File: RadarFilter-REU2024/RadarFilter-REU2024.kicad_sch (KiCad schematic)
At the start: 33 parts, among them J1 73099-0, J2 73099-0, J2 Conn_01x04_Pin, J3 73099-0, J6 CONSMA002, J7 CONSMA002, J8 CONSMA002, J9 CONSMA002, U2 ADA4807-2ARM

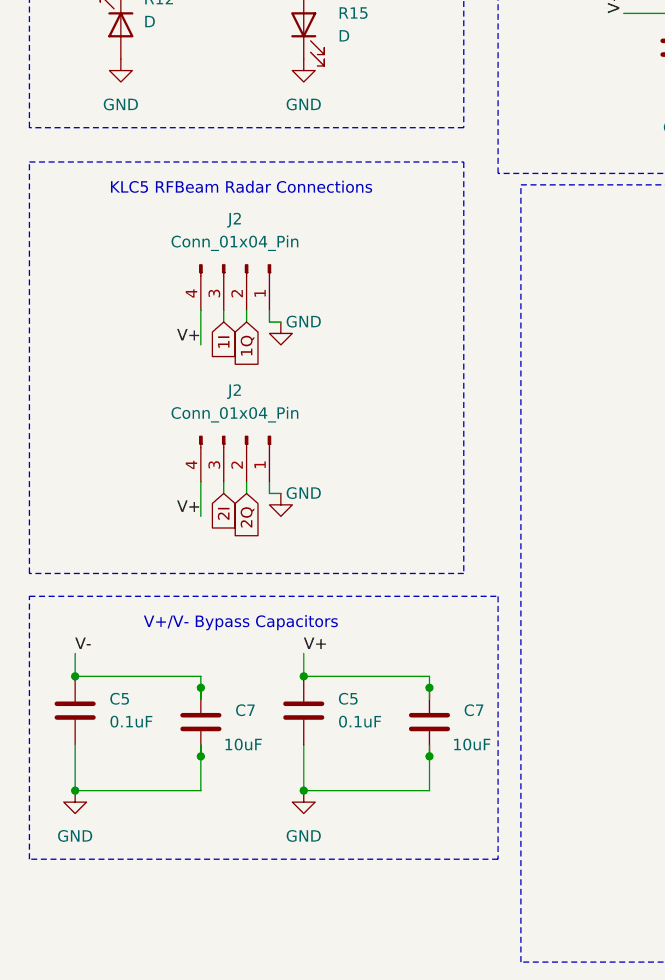
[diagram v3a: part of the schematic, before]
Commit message: added bypass capacitors for KLC5 radar header pins
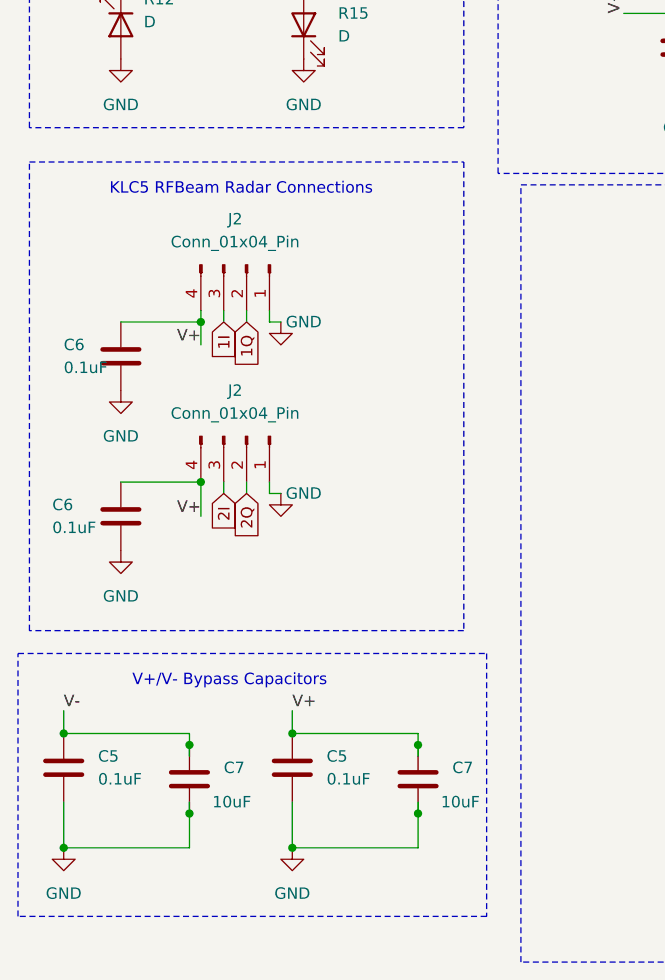
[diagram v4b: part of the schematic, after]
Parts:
- added C6 (x2): 0.1uF, Capacitor_SMD:C_0805_2012Metric_Pad1.18x1.45mm_HandSolder, symbol Device:C
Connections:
- net GND: now also C6.2, C6.2
- net V+: now also C6.1, C6.1
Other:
- moved on the sheet: C5, C7

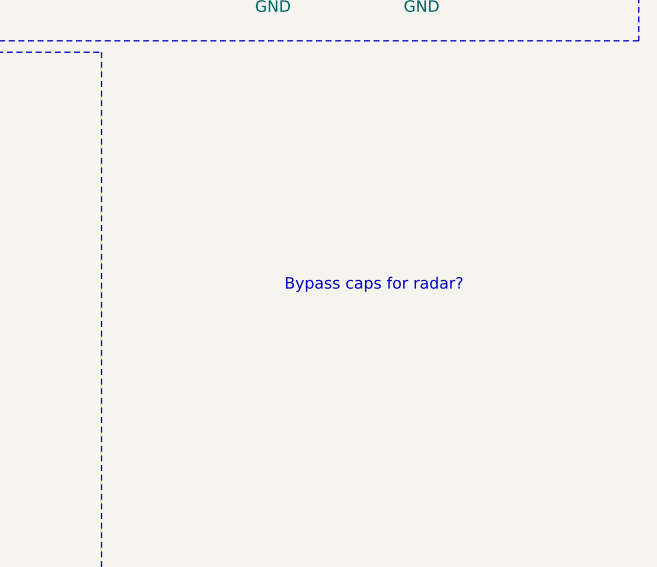
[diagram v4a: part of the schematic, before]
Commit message: adjusted spacing of sma connectors and slight pcb trace modification
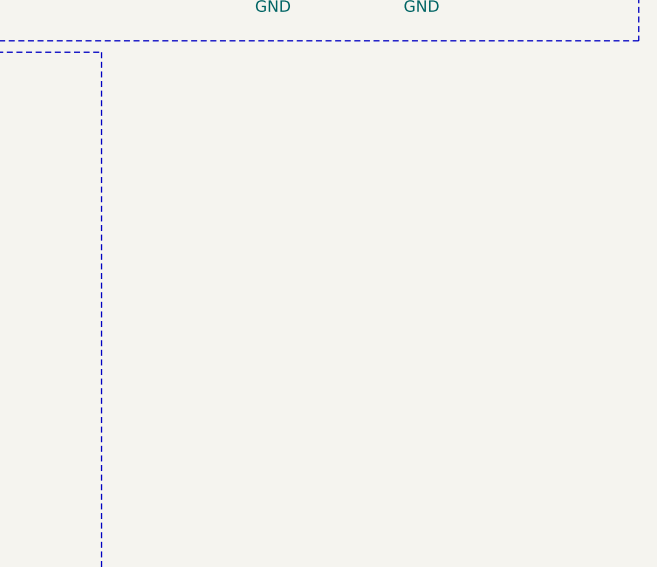
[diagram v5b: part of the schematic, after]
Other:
- note removed: "Bypass caps for radar?"
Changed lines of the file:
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@@
-    (effects (font (size 1.27 1.27)) (justify left bottom))
-  )
-  (text "Bypass caps for radar?" (at 166.37 140.97 0)
     (effects (font (size 1.27 1.27)) (justify left bottom))
   )
